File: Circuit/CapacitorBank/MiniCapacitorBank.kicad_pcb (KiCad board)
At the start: 2 copper layers, 63.5 x 38.1 mm, 46 parts, among them J1 AC Power In, J2 68V out, J3 To Voltage Sensing, Q1 BT138-800, Q2 BT138-800, SW1 SW_Push, U1 PC817, U2 PC817

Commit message: [Circuit] Optimize the layout of PCBs
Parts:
- moved R18 2.54 mm to (61.0, 94.0)
- moved R19 2.54 mm to (63.5, 94.0)
- moved D8 2.54 mm to (66.0, 111.8), turned to 0 degrees
- turned D7 to 180 degrees
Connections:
- D8 pad 2: Net-(D8-Pad2) -> Net-(C1-Pad2)
- Q2 pad 1: Net-(D8-Pad1) -> Net-(Q2-Pad1)
- R20 pad 2: Net-(D8-Pad1) -> Net-(Q2-Pad1)
- R21 pad 1: Net-(C1-Pad2) -> Net-(D8-Pad1)
- R21 pad 2: Net-(D8-Pad2) -> Net-(Q2-Pad1)
- R8 pad 2: Net-(R8-Pad2) -> Net-(C1-Pad2)
- R9 pad 1: Net-(R8-Pad2) -> Net-(C1-Pad2)
- U2 pad 3: Net-(D8-Pad1) -> Net-(Q2-Pad1)
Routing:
- net Net-(D8-Pad1): track 30.2 -> 2.54 mm
- net Net-(Q2-Pad1): track 0.00 -> 22.0 mm
- net Net-(C1-Pad2): track 84.2 -> 103.7 mm
- net Net-(D8-Pad2): track 7.18 -> 0.00 mm
- net Net-(D7-Pad2): track 9.72 -> 3.59 mm
- net Net-(R8-Pad2): track 2.54 -> 0.00 mm

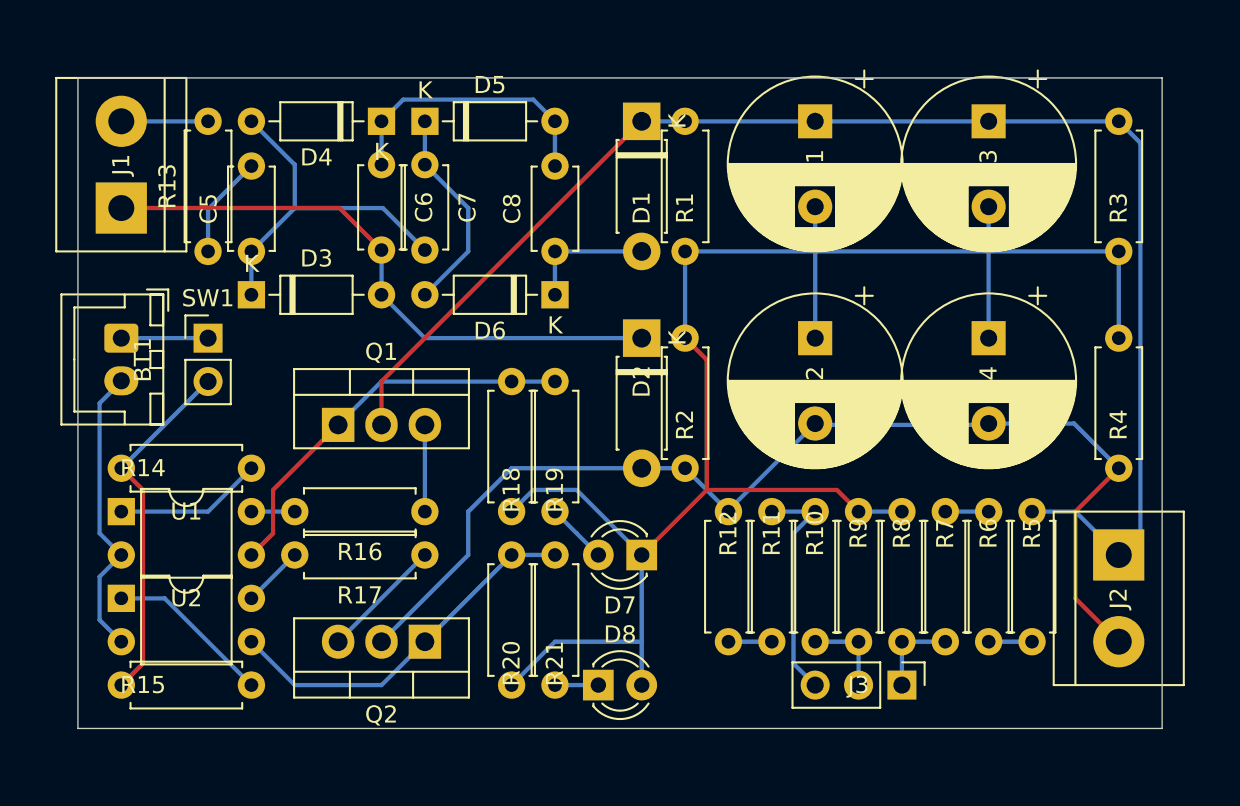
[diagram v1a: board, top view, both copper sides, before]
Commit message: [Circuit] Fine tune some pcb layouts
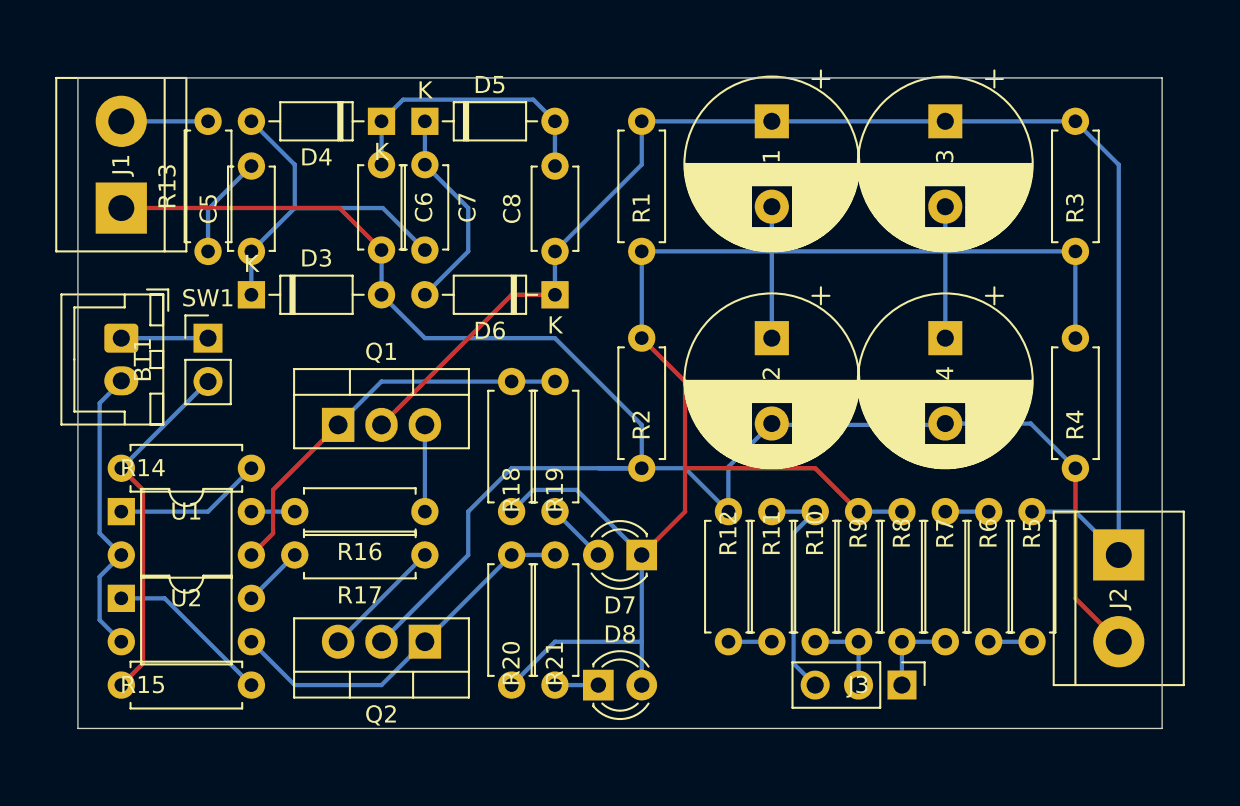
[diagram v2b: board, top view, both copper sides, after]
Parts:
- removed D1, D2: 1N4007, Diode_THT:D_DO-41_SOD81_P7.62mm_Horizontal
- moved C3 2.54 mm to (86.4, 78.7)
- moved C4 2.54 mm to (86.4, 91.4)
- moved R1 2.54 mm to (68.6, 78.7)
- moved R2 2.54 mm to (68.6, 91.4)
- moved C1 2.54 mm to (76.2, 78.7)
- moved C2 2.54 mm to (76.2, 91.4)
- moved R3 2.54 mm to (94.0, 78.7)
- moved R4 2.54 mm to (94.0, 91.4)
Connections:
- C2 pad 2: /PowerOut- -> /ACPowerIn-
- C4 pad 2: /PowerOut- -> /ACPowerIn-
- C8 pad 1: Net-(C8-Pad1) -> /PowerOut+
- D6 pad 1: Net-(C8-Pad1) -> /PowerOut+
- J2 pad 2: /PowerOut- -> /ACPowerIn-
- Q2 pad 2: /PowerOut- -> /ACPowerIn-
- R12 pad 2: /PowerOut- -> /ACPowerIn-
- R2 pad 2: /PowerOut- -> /ACPowerIn-
- R4 pad 2: /PowerOut- -> /ACPowerIn-
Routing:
- net /ACPowerIn-: track 35.2 -> 105.9 mm
- net /PowerOut-: track 65.6 -> 0.00 mm
- net Net-(C8-Pad1): track 7.62 -> 0.00 mm
- net Net-(C1-Pad2): track 103.7 -> 105.5 mm
- net /PowerOut+: track 84.6 -> 83.6 mm

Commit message: [Circuit] Adjust resistors in capacitor bank
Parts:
- R16, R17: value 1K -> 68K
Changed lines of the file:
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@@
       (effects (font (size 1 1) (thickness 0.15)))
     )
-    (fp_text value 1K (at 3.81 2.37) (layer F.Fab)
+    (fp_text value 68K (at 3.81 2.37) (layer F.Fab)
       (effects (font (size 1 1) (thickness 0.15)))
     )
@@
       (effects (font (size 1 1) (thickness 0.15)))
     )
-    (fp_text value 1K (at 3.81 2.37) (layer F.Fab)
+    (fp_text value 68K (at 3.81 2.37) (layer F.Fab)
       (effects (font (size 1 1) (thickness 0.15)))
     )

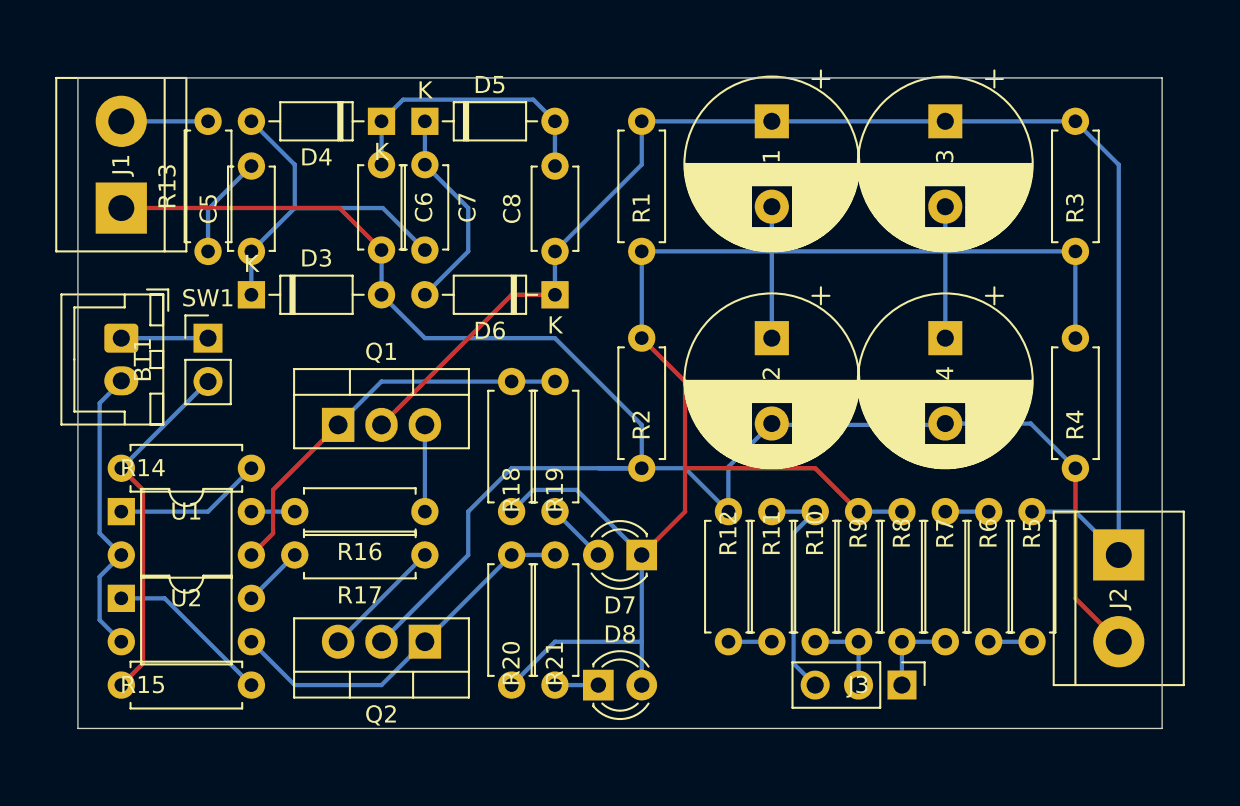
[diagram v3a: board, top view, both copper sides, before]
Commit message: [Circuit] Adjust the resistors in capacitor bank, again
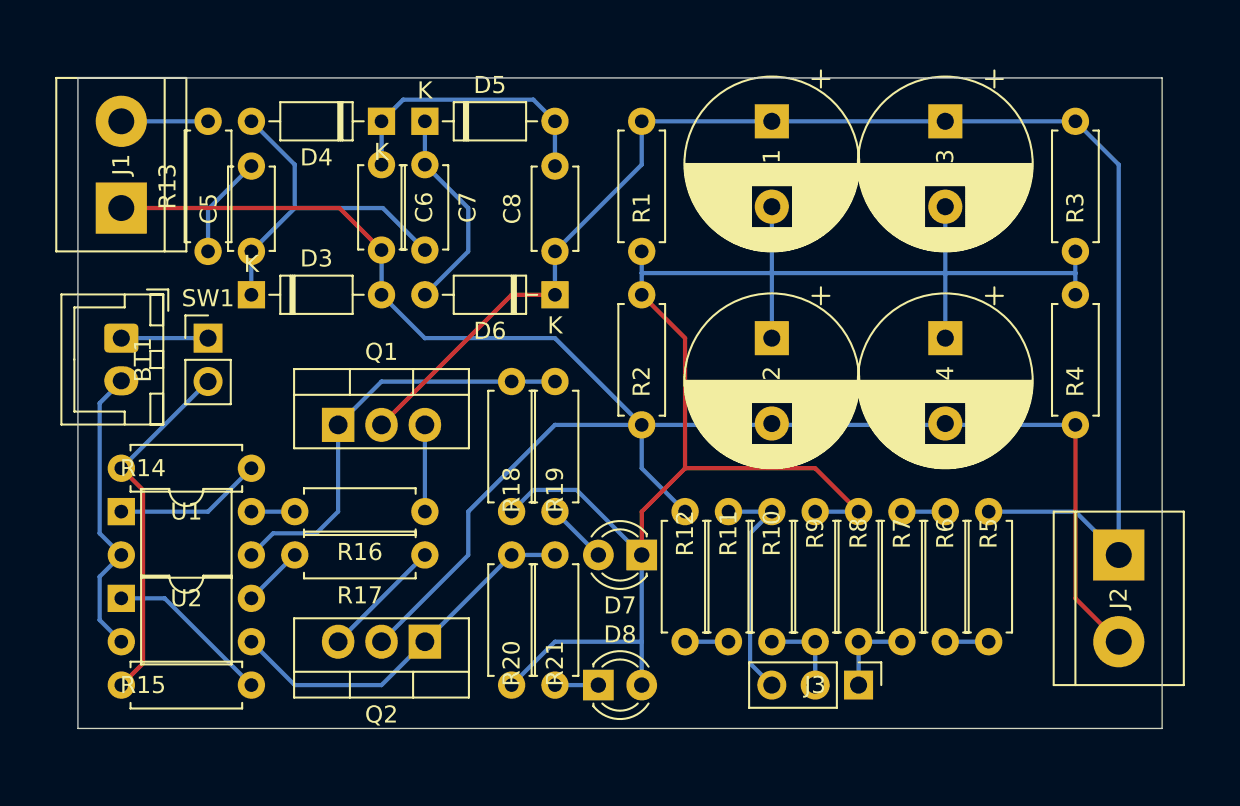
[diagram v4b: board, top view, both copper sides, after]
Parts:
- R16, R17: value 68K -> 3.3K
- moved R11 2.54 mm to (73.7, 101.6)
- moved R6 2.54 mm to (86.4, 109.2)
- moved R7 2.54 mm to (83.8, 101.6)
- moved R9 2.54 mm to (78.7, 101.6)
- moved J3 2.54 mm to (81.3, 111.8)
- moved R10 2.54 mm to (76.2, 109.2)
- moved R12 2.54 mm to (71.1, 109.2)
- moved R2 2.54 mm to (68.6, 88.9)
- moved R4 2.54 mm to (94.0, 88.9)
- moved R5 2.54 mm to (88.9, 101.6)
- moved R8 2.54 mm to (81.3, 109.2)
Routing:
- net /PowerOut+: track 83.6 -> 86.1 mm
- net Net-(C1-Pad2): track 105.5 -> 103.0 mm
- net Net-(Q1-Pad1): track 23.5 -> 25.0 mm
- net /ACPowerIn-: track 105.9 -> 104.6 mm

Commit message: [Circuit] Adjust footprint of customized components and optimize the PCB design
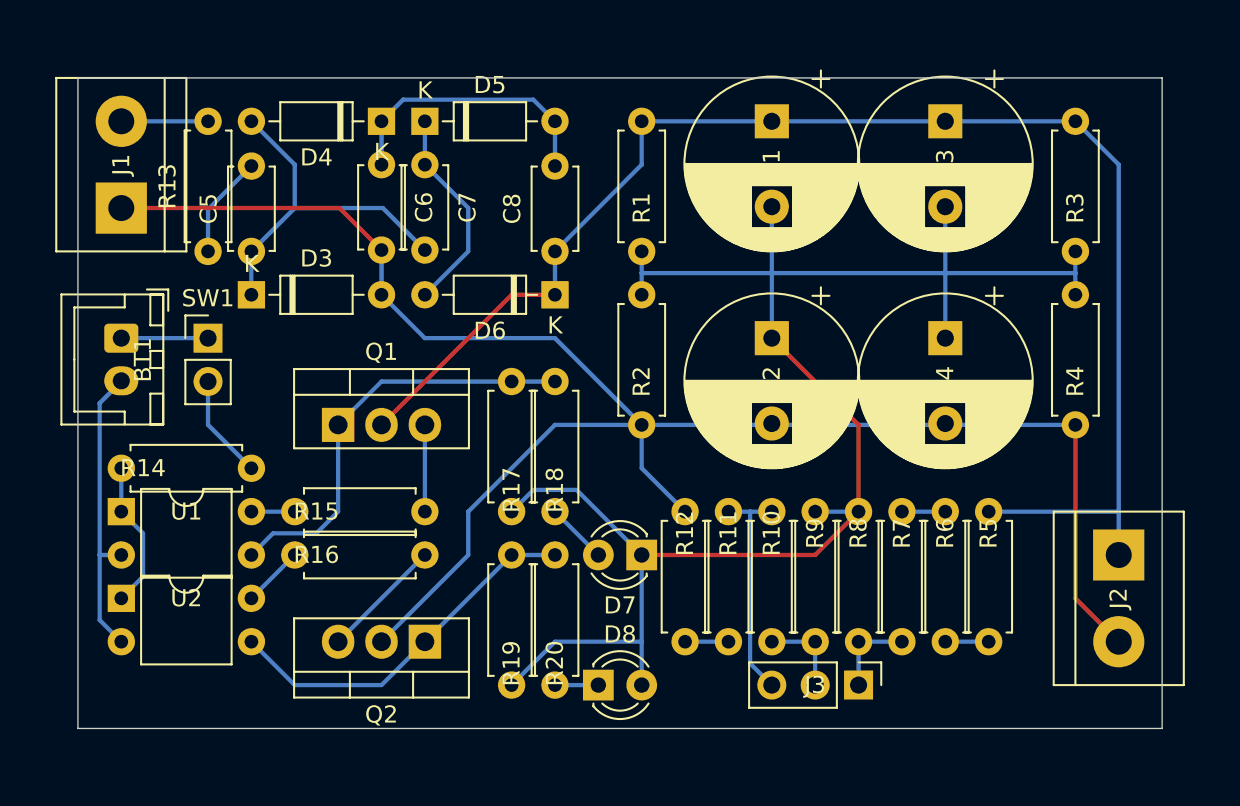
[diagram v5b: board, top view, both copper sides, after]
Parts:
- removed the R15 at (38.1, 111.8)
- R14: value 1K -> 510
- moved R14 7.62 mm to (45.7, 99.1), turned to 180 degrees
- renumbered R16 to R15, R17 to R16, R18 to R17, R19 to R18, R20 to R19, R21 to R20
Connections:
- U2 pad 1: Net-(R15-Pad2) (its old number) -> Net-(R14-Pad2)
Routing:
- net Net-(R14-Pad1): track 20.9 -> 6.13 mm
- net Net-(R15-Pad2) (its old number): track 9.72 -> 0.00 mm
- net Net-(C1-Pad2): track 103.0 -> 100.5 mm
- net /PowerOut+: track 86.1 -> 85.1 mm
- net /Sensor0V: track 13.8 -> 13.2 mm

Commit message: [Circuit] Add screw holes to PCBs
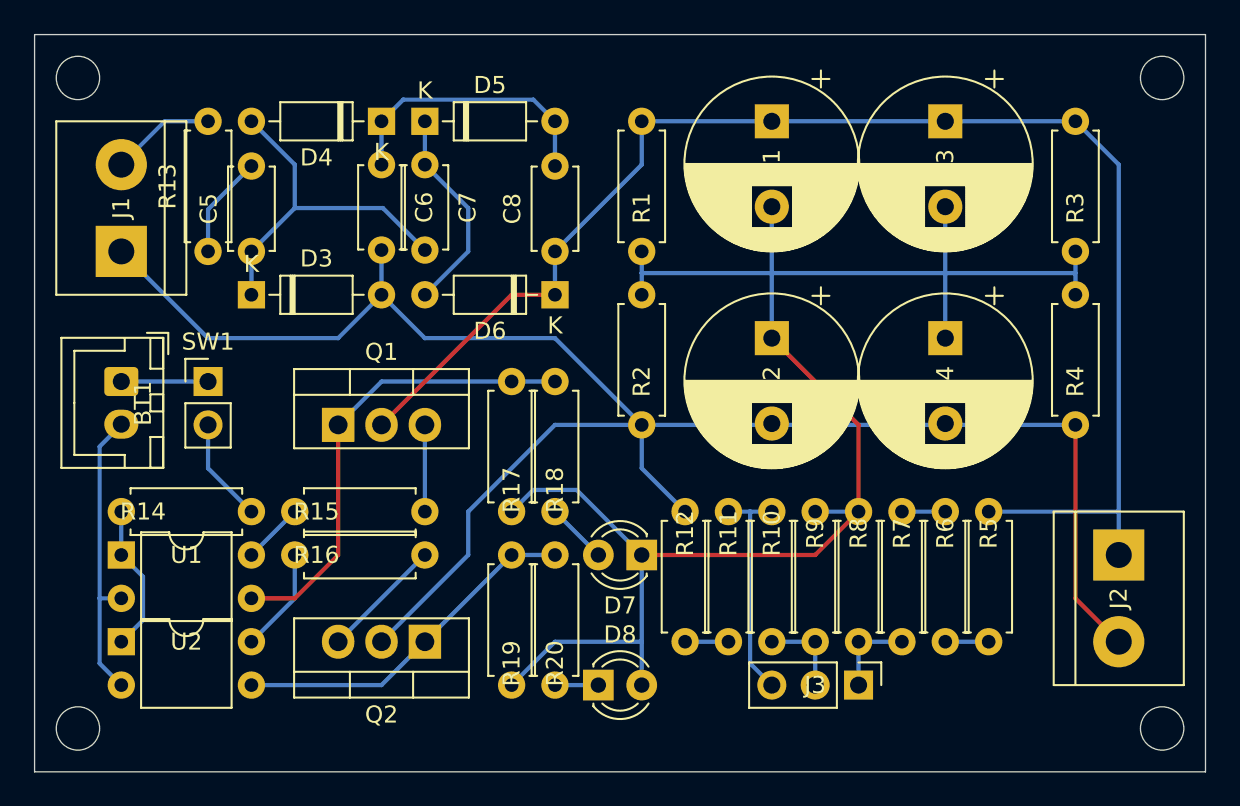
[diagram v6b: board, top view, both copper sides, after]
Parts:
- moved BT1 2.54 mm to (38.1, 94.0)
- moved J1 2.54 mm to (38.1, 86.4)
- moved SW1 2.54 mm to (43.2, 94.0)
- moved U1 2.54 mm to (38.1, 104.1)
- moved R14 2.54 mm to (45.7, 101.6)
- moved U2 2.54 mm to (38.1, 109.2)
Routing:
- net Net-(Q1-Pad1): track 25.0 -> 27.5 mm
- net Net-(R16-Pad2): track 3.59 -> 6.13 mm
- net /ACPowerIn-: track 104.6 -> 106.7 mm
- net Net-(R15-Pad2): track 2.54 -> 3.59 mm
- net /ACPowerIn+: track 5.16 -> 6.21 mm
- net Net-(Q2-Pad1): track 22.0 -> 20.9 mm
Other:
- board size 63.5 x 38.1 mm -> 68.6 x 43.2 mm

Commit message: [Circuit] One channel voltage sensing and control modules
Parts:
- J3: footprint Connector_PinHeader_2.54mm:PinHeader_1x03_P2.54mm_Vertical -> Connector_PinHeader_2.54mm:PinHeader_1x02_P2.54mm_Vertical
- renumbered R18 to R19, R19 to R20, R20 to R21
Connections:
- J3 pad 2: /Sensor3V -> /Sensor0V
- R10 pad 1: /Sensor3V -> Net-(R10-Pad1)
- R9 pad 2: /Sensor3V -> Net-(R10-Pad1)
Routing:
- net /Sensor3V: track 5.08 -> 0.00 mm
- net Net-(R10-Pad1): track 0.00 -> 2.54 mm
- net /Sensor0V: track 13.2 -> 15.8 mm

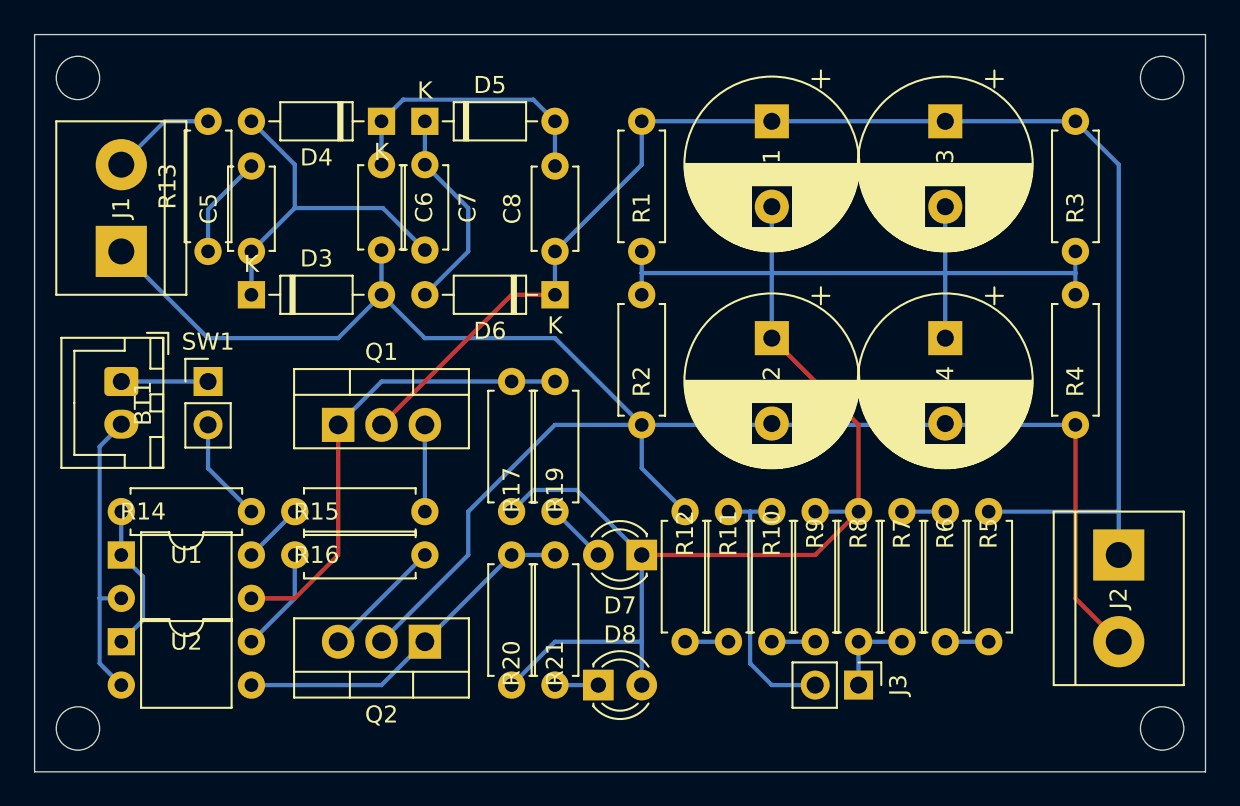
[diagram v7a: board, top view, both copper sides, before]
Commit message: [Circuit] Add a discharge signal to capacitor bank
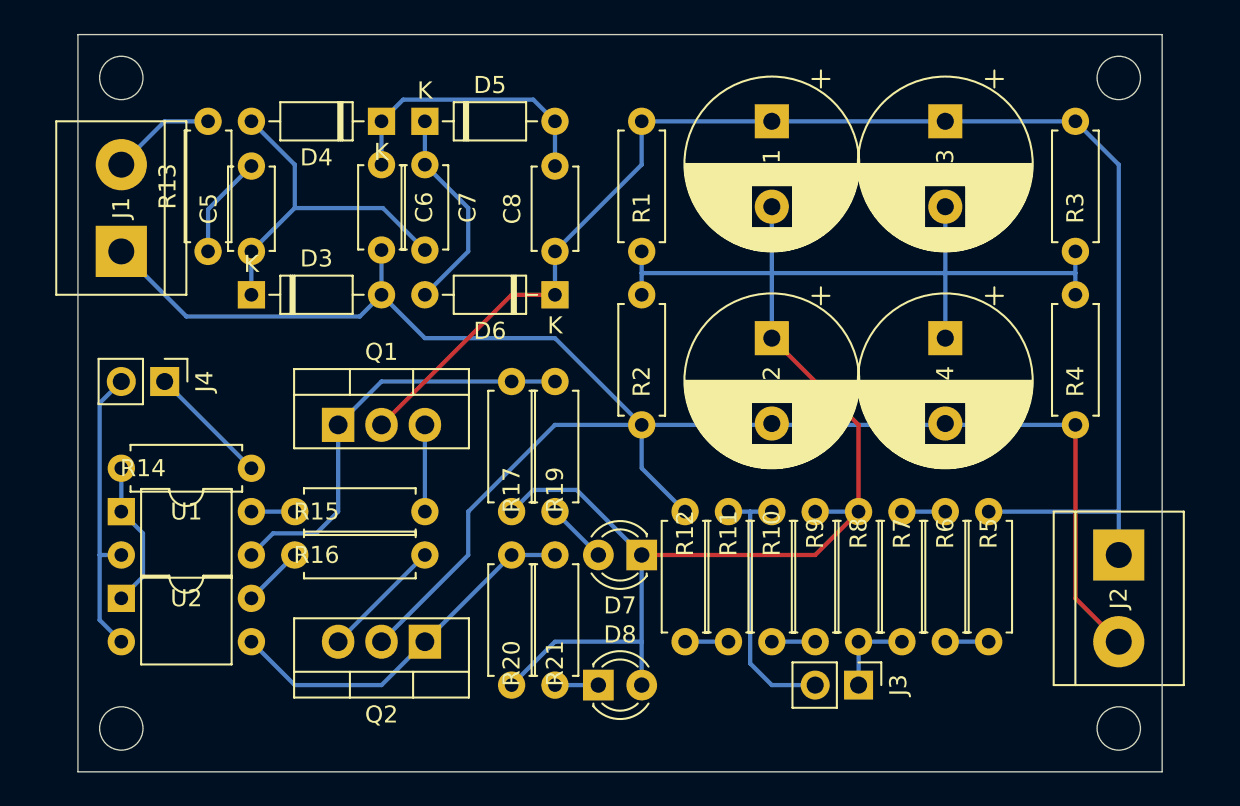
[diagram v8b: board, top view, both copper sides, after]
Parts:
- removed BT1: 12V Battery, Connector_JST:JST_XH_B2B-XH-A_1x02_P2.50mm_Vertical
- removed SW1: SW_Push, Connector_PinHeader_2.54mm:PinHeader_1x02_P2.54mm_Vertical
- added J4: Discharge Signal, Connector_PinHeader_2.54mm:PinHeader_1x02_P2.54mm_Vertical, F.Cu at (40.6, 94.0)
- moved U1 2.54 mm to (38.1, 101.6)
- moved R14 2.54 mm to (45.7, 99.1)
- moved U2 2.54 mm to (38.1, 106.7)
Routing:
- net Net-(BT1-Pad1): track 5.08 -> 0.00 mm
- net Net-(Q1-Pad1): track 27.5 -> 25.0 mm
- net Net-(R16-Pad2): track 6.13 -> 3.59 mm
- net /ACPowerIn-: track 106.7 -> 105.7 mm
- net Net-(Q2-Pad1): track 20.9 -> 22.0 mm
- net Net-(R15-Pad2): track 3.59 -> 2.54 mm
- net Net-(J4-Pad1): track 6.13 -> 7.18 mm
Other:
- board size 68.6 x 43.2 mm -> 63.5 x 43.2 mm
